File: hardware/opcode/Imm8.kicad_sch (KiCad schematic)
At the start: 2 parts, among them U17 74HC597

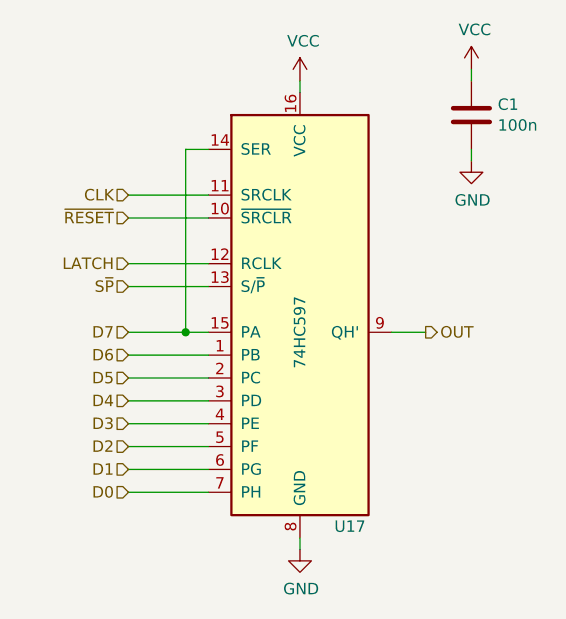
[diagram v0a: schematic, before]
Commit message: Update all to Kicad 6
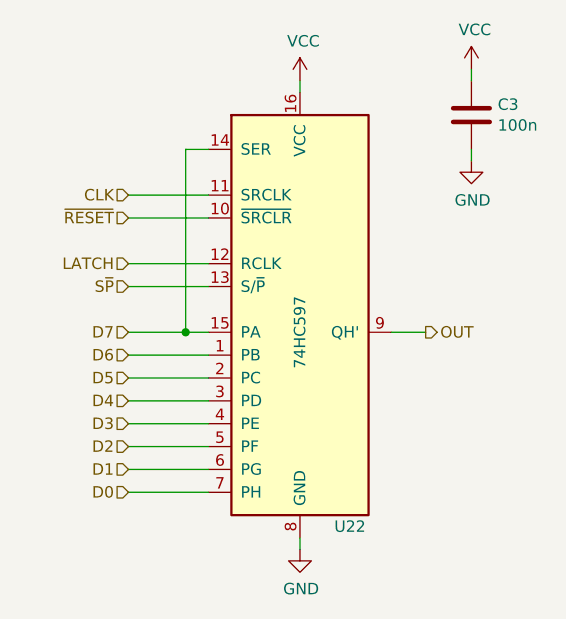
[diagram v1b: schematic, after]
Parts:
- renumbered C1 to C3, U17 to U22
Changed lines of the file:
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@@
   (symbol (lib_id "power:GND") (at 87.63 104.14 0) (unit 1)
     (in_bom yes) (on_board yes)
-    (property "Reference" "#PWR0134" (id 0) (at 87.63 110.49 0)
+    (property "Reference" "#PWR045" (id 0) (at 87.63 110.49 0)
       (effects (font (size 1.27 1.27)) hide)
     )
@@
   (symbol (lib_id "riscv-serial:74HC597") (at 87.63 80.01 0) (unit 1)
     (in_bom yes) (on_board yes)
-    (property "Reference" "U17" (id 0) (at 91.44 101.6 0)
+    (property "Reference" "U22" (id 0) (at 91.44 101.6 0)
       (effects (font (size 1.27 1.27)) (justify left))
     )
@@
   (symbol (lib_id "power:VCC") (at 87.63 52.07 0) (unit 1)
     (in_bom yes) (on_board yes)
-    (property "Reference" "#PWR0133" (id 0) (at 87.63 55.88 0)
+    (property "Reference" "#PWR043" (id 0) (at 87.63 55.88 0)
       (effects (font (size 1.27 1.27)) hide)
     )
@@
   (symbol (lib_id "Device:C") (at 106.68 55.88 0) (unit 1)
     (in_bom yes) (on_board yes)
-    (property "Reference" "C1" (id 0) (at 109.601 54.7116 0)
+    (property "Reference" "C3" (id 0) (at 109.601 54.7116 0)
       (effects (font (size 1.27 1.27)) (justify left))
     )
@@
   (symbol (lib_id "power:VCC") (at 106.68 50.8 0) (unit 1)
     (in_bom yes) (on_board yes)
-    (property "Reference" "#PWR0135" (id 0) (at 106.68 54.61 0)
+    (property "Reference" "#PWR042" (id 0) (at 106.68 54.61 0)
       (effects (font (size 1.27 1.27)) hide)
     )
@@
   (symbol (lib_id "power:GND") (at 106.68 60.96 0) (unit 1)
     (in_bom yes) (on_board yes)
-    (property "Reference" "#PWR0136" (id 0) (at 106.68 67.31 0)
+    (property "Reference" "#PWR044" (id 0) (at 106.68 67.31 0)
       (effects (font (size 1.27 1.27)) hide)
     )
